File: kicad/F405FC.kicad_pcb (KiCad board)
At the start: 4 copper layers, 36 x 36 mm, 161 parts, among them J1 USB4105-GF-A, J2 ESC, J3 HD VTX, J4 GPS, J5 ELRS, P1 VBAT, P10 LED_DIN, P11 5V, P12 GND, P13 5V, P14 BUZ_N, P15 UART5_TX, P16 UART5_RX, P17 UART6_TX, P18 UART6_RX, P19 MOTOR5, P2 GND, P20 MOTOR6, P21 MOTOR7, P22 MOTOR8, P23 RSSI_IN, P24 GND, P25 5V, P3 10V, P4 GND, P5 CAM1_VID, P6 CAM2_VID, P7 VTX_VID, P8 5V, P9 GND, Q1 PMV40UN2, Q2 NX7002AK, SW1 BOOT, U1 LMR38020FSDDAR, U10 W25N01GV, U11 TS5A3159A, U12 SN74LV1T125, U13 USBLC6-2SC6, U2 LMR38020FSDDAR, U3 STM32F405RGT6, U4 LP38692MP-3.3, U5 LP5907MFX-3.3, U6 ICM-42688-P, U7 BMI270, U8 BMP390, U9 IIS2MDC, Y1 8MHz

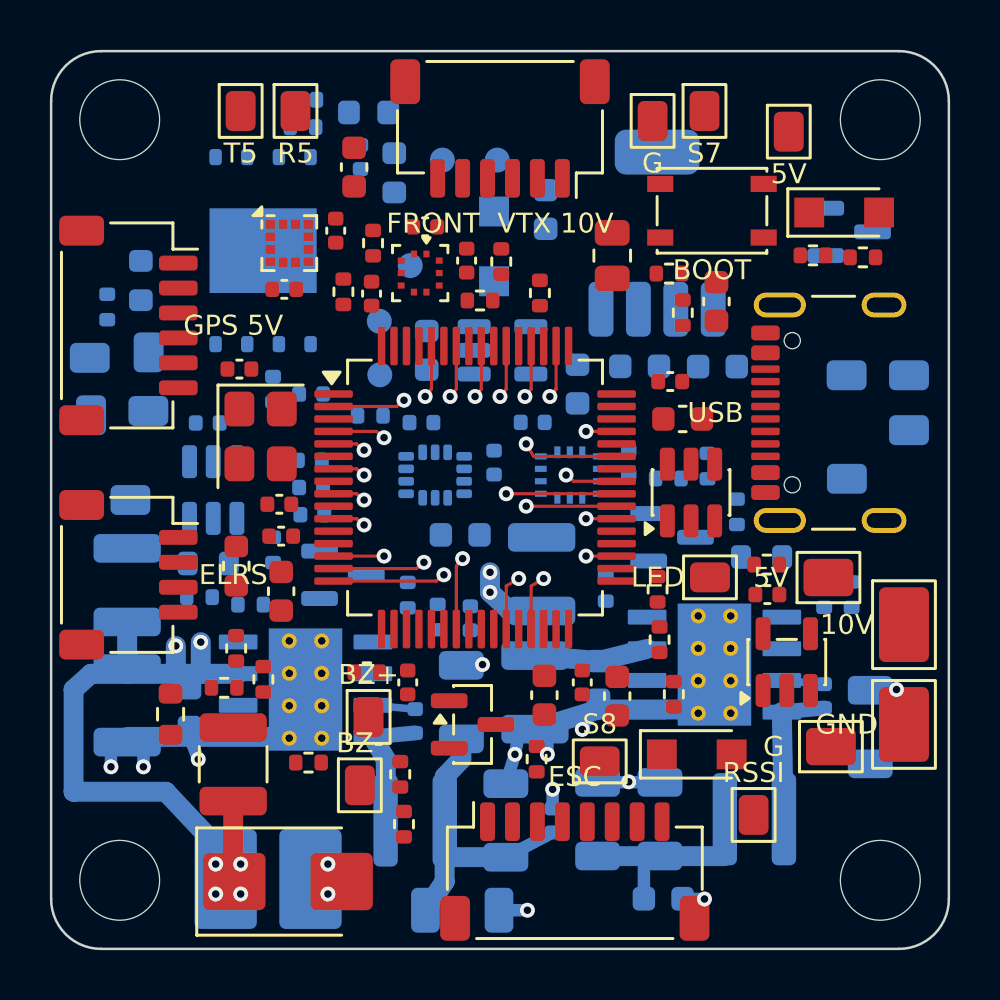
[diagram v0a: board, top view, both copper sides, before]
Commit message: Gate 3 re-review fixes: rule-based labels + regular pad grids, VBAT In2 zone, MCU routing ring/decap offsets, U13/D9 moves, P12 removed (D-21)
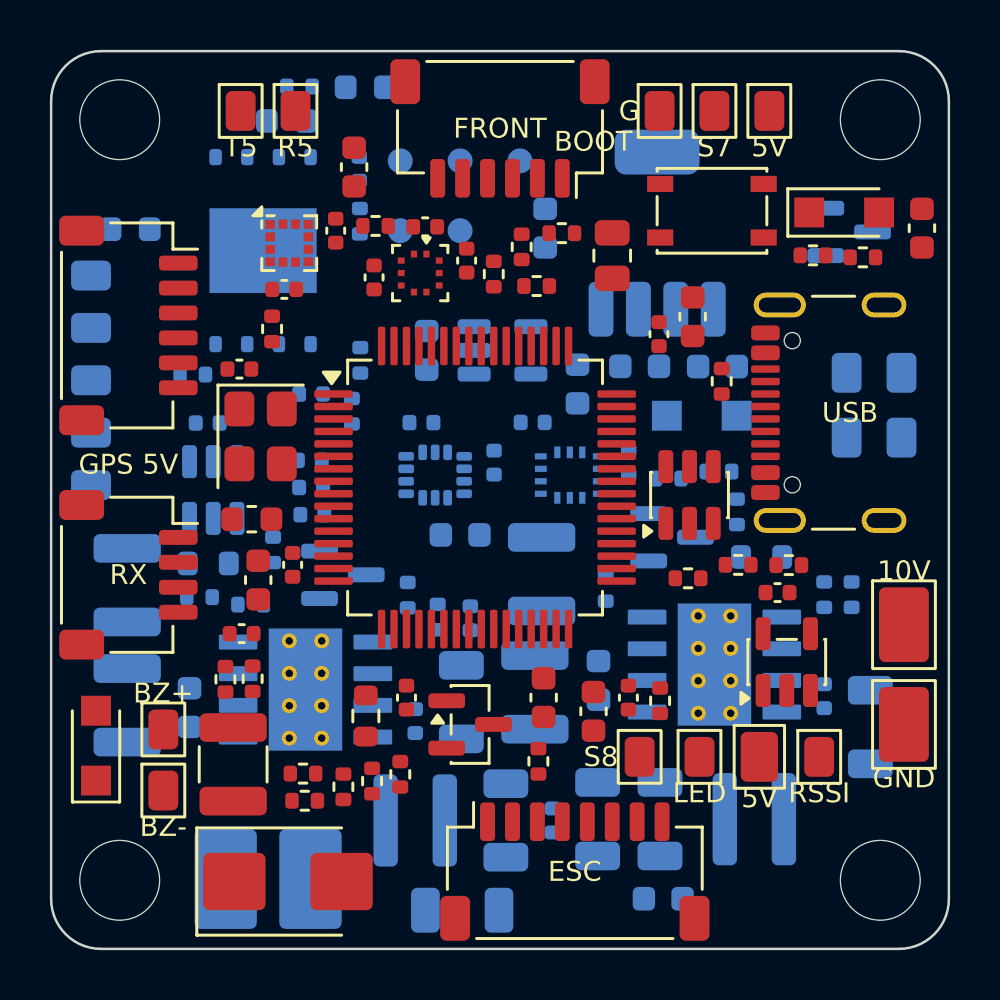
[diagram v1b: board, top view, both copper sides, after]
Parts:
- removed P12: GND, F405FC:Pad_SMD_1.5x2.0mm
- moved D9 24.1 mm to (101.8, 127.8), turned to 90 degrees
- moved D5 10.7 mm to (126.1, 114.6), turned to 0 degrees
- moved C51 8.75 mm to (134.9, 107.1)
- moved P13 8.25 mm to (104.5, 127.2)
- moved P14 7.88 mm to (104.5, 129.7)
- moved R14 7.83 mm to (112.6, 126.7)
- moved P11 7.71 mm to (128.4, 128.3), turned to 0 degrees
- moved P10 7.21 mm to (126.0, 128.3), turned to 0 degrees
- moved P9 7.08 mm to (101.6, 111.1)
- moved TP5 6.62 mm to (116.4, 107.2)
- moved TP3 6.08 mm to (118.8, 104.4)
- moved P8 5.90 mm to (101.6, 109.0)
- moved P7 5.80 mm to (101.6, 117.4), turned to 90 degrees
- moved R32 5.80 mm to (127.5, 120.6), turned to 180 degrees
- moved C37 5.41 mm to (107.6, 123.4)
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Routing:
- net VBAT: track 48.1 -> 0.00 mm, vias 8 -> 0
- net GND: track 26.6 -> 0.00 mm, vias 14 -> 0
- net 5V: track 10.5 -> 0.00 mm
- net 10V: track 6.81 -> 0.00 mm
- net SW_10V: track 6.01 -> 0.00 mm
- net SW_5V: track 5.20 -> 0.00 mm
- net UART2_TX: track 4.52 -> 0.00 mm, vias 1 -> 0
- net MOTOR6: track 4.42 -> 0.00 mm, vias 1 -> 0
- net UART1_RX: track 3.91 -> 0.00 mm, vias 1 -> 0
- net ESC_TLM: track 3.72 -> 0.00 mm, vias 1 -> 0
- net MOTOR5: track 3.62 -> 0.00 mm, vias 1 -> 0
- net CAM_SEL: track 2.92 -> 0.00 mm, vias 1 -> 0
- net SPI1_MOSI: track 2.92 -> 0.00 mm, vias 1 -> 0
- net MOTOR3: track 2.31 -> 0.00 mm, vias 1 -> 0
- net MOTOR2: track 2.31 -> 0.00 mm, vias 1 -> 0
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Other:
- board text added: "FRONT"
- board text added: "RX"
- board text removed: "ELRS"
- board text removed: "FRONT VTX 10V"

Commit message: Routing: PathFinder router, reachability pre-check, fanout stub crossing fix + IMU via keepout
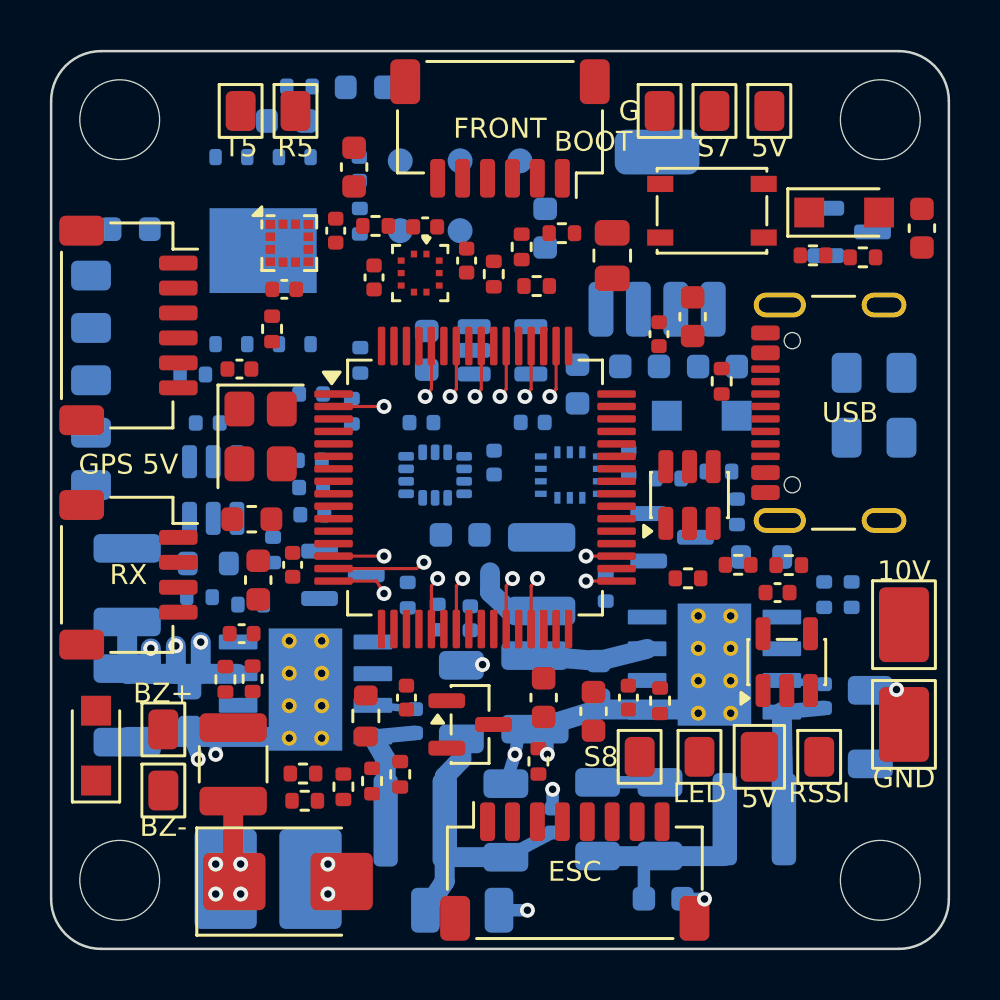
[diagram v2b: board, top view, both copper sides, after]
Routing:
- net GND: track 0.00 -> 24.6 mm, vias 0 -> 11
- net VBAT: track 0.00 -> 22.0 mm, vias 0 -> 7
- net 5V: track 0.00 -> 10.5 mm
- net 10V: track 0.00 -> 6.81 mm
- net SW_10V: track 0.00 -> 6.01 mm
- net SW_5V: track 0.00 -> 5.20 mm
- net ESC_TLM: track 0.00 -> 3.72 mm, vias 0 -> 1
- net UART2_TX: track 0.00 -> 2.31 mm, vias 0 -> 1
- net UART5_RX: track 0.00 -> 2.12 mm, vias 0 -> 1
- net UART3_RX: track 0.00 -> 2.12 mm, vias 0 -> 1
- net SPI3_MISO: track 0.00 -> 2.12 mm, vias 0 -> 1
- net GYRO2_CS: track 0.00 -> 2.12 mm, vias 0 -> 1
- net FLASH_CS: track 0.00 -> 2.12 mm, vias 0 -> 1
- net BOOT0: track 0.00 -> 2.12 mm, vias 0 -> 1
- net SPI1_SCK: track 0.00 -> 2.12 mm, vias 0 -> 1
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- added copper zone on In1.Cu, net GND
- added copper zone on In2.Cu, net VBAT

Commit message: PathFinder: conservative grid margins, string pulling, cost-based window choice, optional In1 hops; power.md §5 rev C; current-limit floors in script (G3R-08)
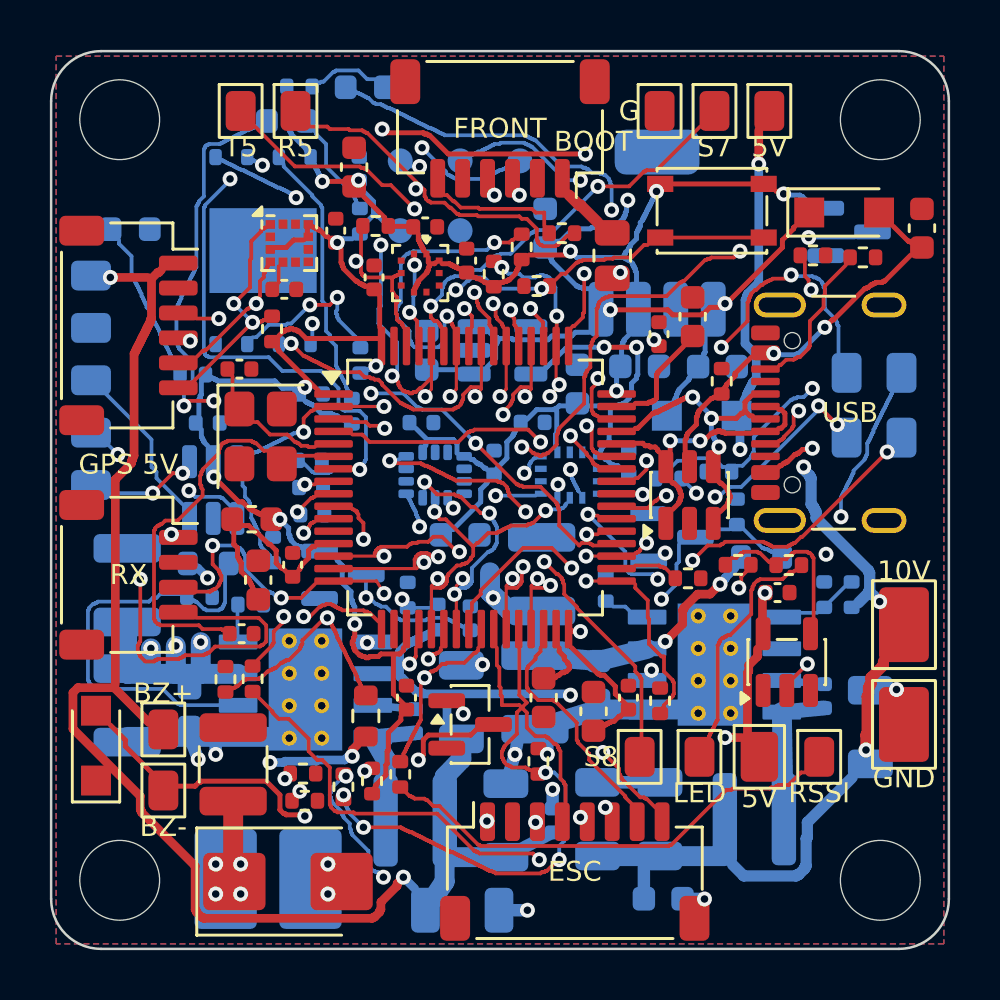
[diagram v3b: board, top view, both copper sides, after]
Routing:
- net 5V: track 10.5 -> 95.0 mm, vias 0 -> 7
- net 3V3: track 0.00 -> 82.3 mm, vias 0 -> 14
- net 5V_SYS: track 0.00 -> 58.6 mm, vias 0 -> 6
- net CURR_ADC: track 0.00 -> 47.3 mm, vias 0 -> 5
- net STATUS_LED_GREEN: track 0.00 -> 33.6 mm, vias 0 -> 4
- net NRST: track 0.00 -> 32.5 mm, vias 0 -> 3
- net 10V: track 6.81 -> 36.2 mm, vias 0 -> 4
- net STATUS_LED_BLUE: track 1.22 -> 29.3 mm, vias 1 -> 3
- net UART2_RX: track 0.00 -> 23.5 mm, vias 0 -> 2
- net BOOT0: track 2.12 -> 25.2 mm, vias 1 -> 5
- net 3V3_IMU: track 0.00 -> 22.9 mm, vias 0 -> 2
- net VTX_OFF_G: track 0.00 -> 21.8 mm, vias 0 -> 3
- net BEEPER: track 0.00 -> 21.0 mm, vias 0 -> 4
- net UART5_RX: track 2.12 -> 23.0 mm, vias 1 -> 3
- net ESC_TLM: track 3.72 -> 22.7 mm, vias 1 -> 3
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- added copper zone on B.Cu, net GND
- added copper zone on F.Cu, net GND
- added copper zone on In2.Cu, net GND

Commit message: Placement tweaks for routability (U5/C23/C53/R21/R22), pairwise clearance + hole clearance in router, GND plane-tie pass, route pipeline script
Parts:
- C53: moved to F.Cu
- R21, R22: moved to B.Cu
- moved R21 14.1 mm to (108.6, 114.9), turned to 180 degrees
- moved R22 13.0 mm to (108.8, 117.1), turned to 90 degrees
- moved C53 6.89 mm to (113.0, 128.5)
- moved R14 3.32 mm to (110.5, 129.2), turned to 180 degrees
- moved R18 2.86 mm to (113.1, 126.4)
- moved R40 2.86 mm to (114.2, 131.0)
- moved U5 1.66 mm to (118.5, 110.4)
- moved C23 1.46 mm to (119.7, 113.0), turned to 0 degrees
- moved C22 1.23 mm to (115.6, 110.9)
- moved C42 0.94 mm to (120.2, 114.9)
- moved C18 0.15 mm to (119.7, 107.1)
- moved R39 0.10 mm to (114.1, 129.0)
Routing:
- net 5V: track 95.0 -> 10.5 mm, vias 7 -> 0
- net 3V3: track 82.3 -> 0.00 mm, vias 14 -> 0
- net 5V_SYS: track 58.6 -> 0.00 mm, vias 6 -> 0
- net CURR_ADC: track 47.3 -> 0.00 mm, vias 5 -> 0
- net STATUS_LED_GREEN: track 33.6 -> 0.00 mm, vias 4 -> 0
- net NRST: track 32.5 -> 0.00 mm, vias 3 -> 0
- net 10V: track 36.2 -> 6.81 mm, vias 4 -> 0
- net STATUS_LED_BLUE: track 29.3 -> 1.22 mm, vias 3 -> 1
- net BOOT0: track 25.2 -> 0.00 mm, vias 5 -> 0
- net UART2_RX: track 23.5 -> 0.00 mm, vias 2 -> 0
- net 3V3_IMU: track 22.9 -> 0.00 mm, vias 2 -> 0
- net VTX_OFF_G: track 21.8 -> 0.00 mm, vias 3 -> 0
- net BEEPER: track 21.0 -> 0.00 mm, vias 4 -> 0
- net UART5_RX: track 23.0 -> 2.12 mm, vias 3 -> 1
- net FLASH_CS: track 19.7 -> 0.00 mm, vias 4 -> 0
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- removed copper zone on B.Cu, net GND
- removed copper zone on F.Cu, net GND
- removed copper zone on In2.Cu, net GND

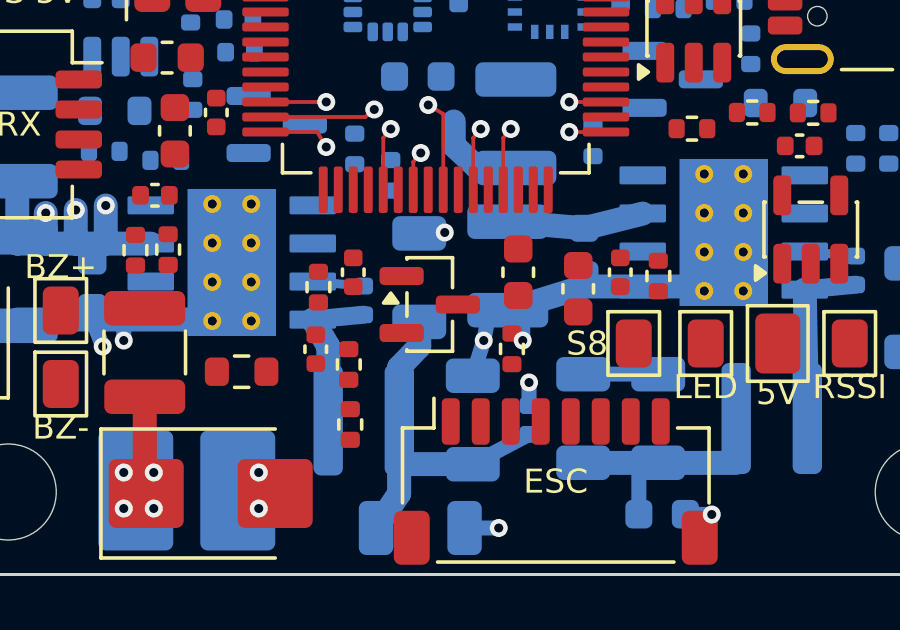
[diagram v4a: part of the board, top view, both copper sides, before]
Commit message: Legalizer keeps non-anchored parts off scripted critical copper; narrower lower VBAT riser; configurable routing grid
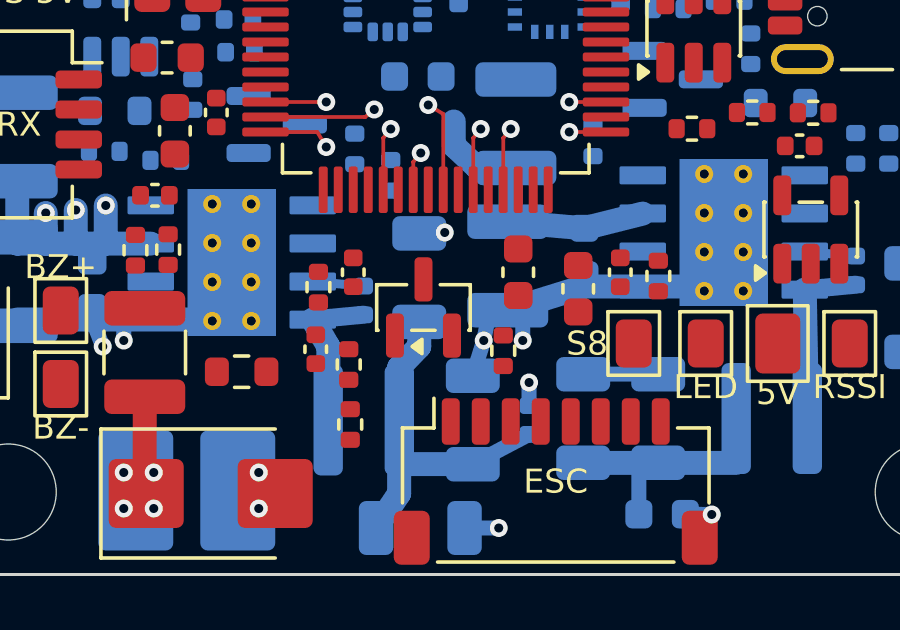
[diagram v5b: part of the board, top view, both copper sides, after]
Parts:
- moved R17 0.30 mm to (119.2, 128.5)
- moved Q1 0.23 mm to (116.6, 127.1), turned to 90 degrees

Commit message: D-23: ADC clamp diodes removed (routing space under the MCU corner); BOM $174.68; PathFinder RESET_NETS
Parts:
- removed D7, D8: BAT54S, Package_TO_SOT_SMD:SOT-23
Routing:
- net ESC_TLM: track 3.72 -> 1.32 mm
- net UART2_TX: track 2.31 -> 0.00 mm, vias 1 -> 0
- net SPI1_MISO: track 0.00 -> 2.31 mm, vias 0 -> 1
- net SPI1_MOSI: track 1.32 -> 0.00 mm, vias 1 -> 0
- net UART2_RX: track 0.00 -> 1.22 mm, vias 0 -> 1
- net GYRO1_INT: track 0.00 -> 1.22 mm, vias 0 -> 1

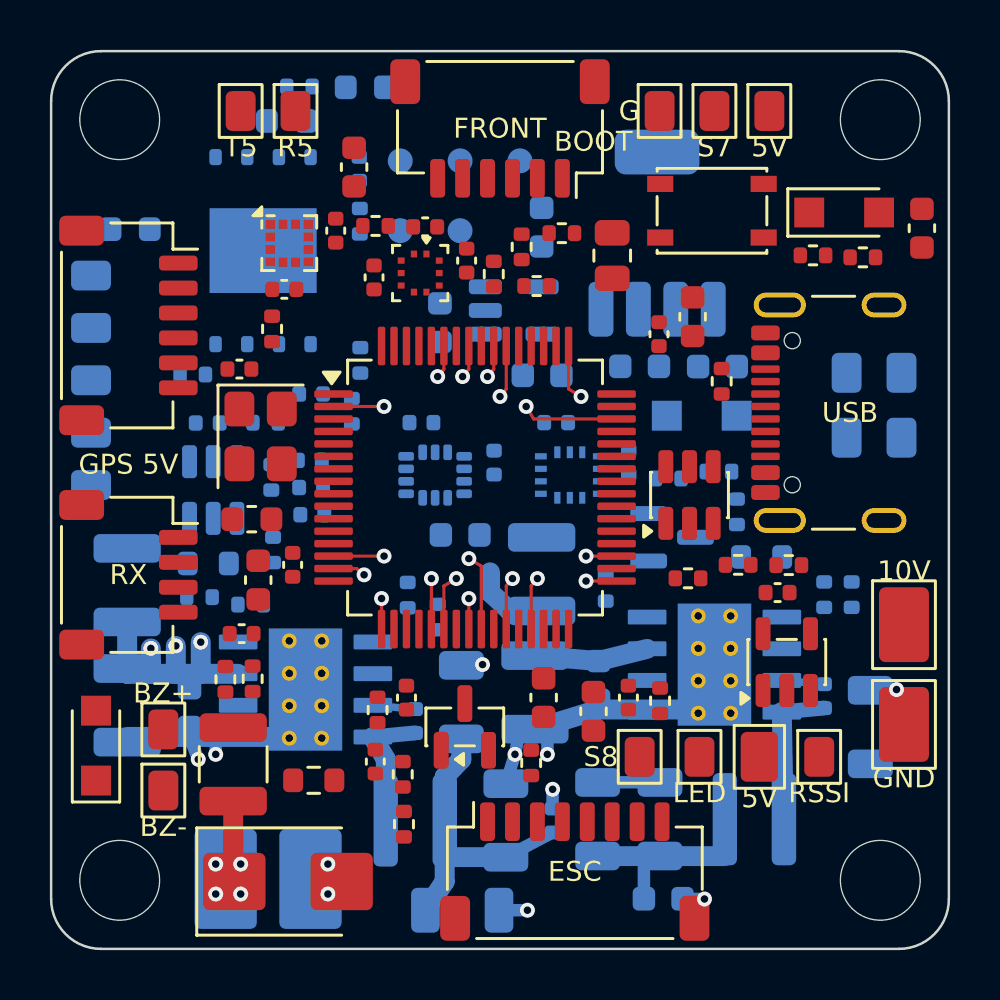
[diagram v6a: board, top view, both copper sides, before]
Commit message: Routing: PathFinder router, fine grid + In1 hops, GND pass, solid SMD pour connections (WIP: 2 DRC errors, 26 opens)
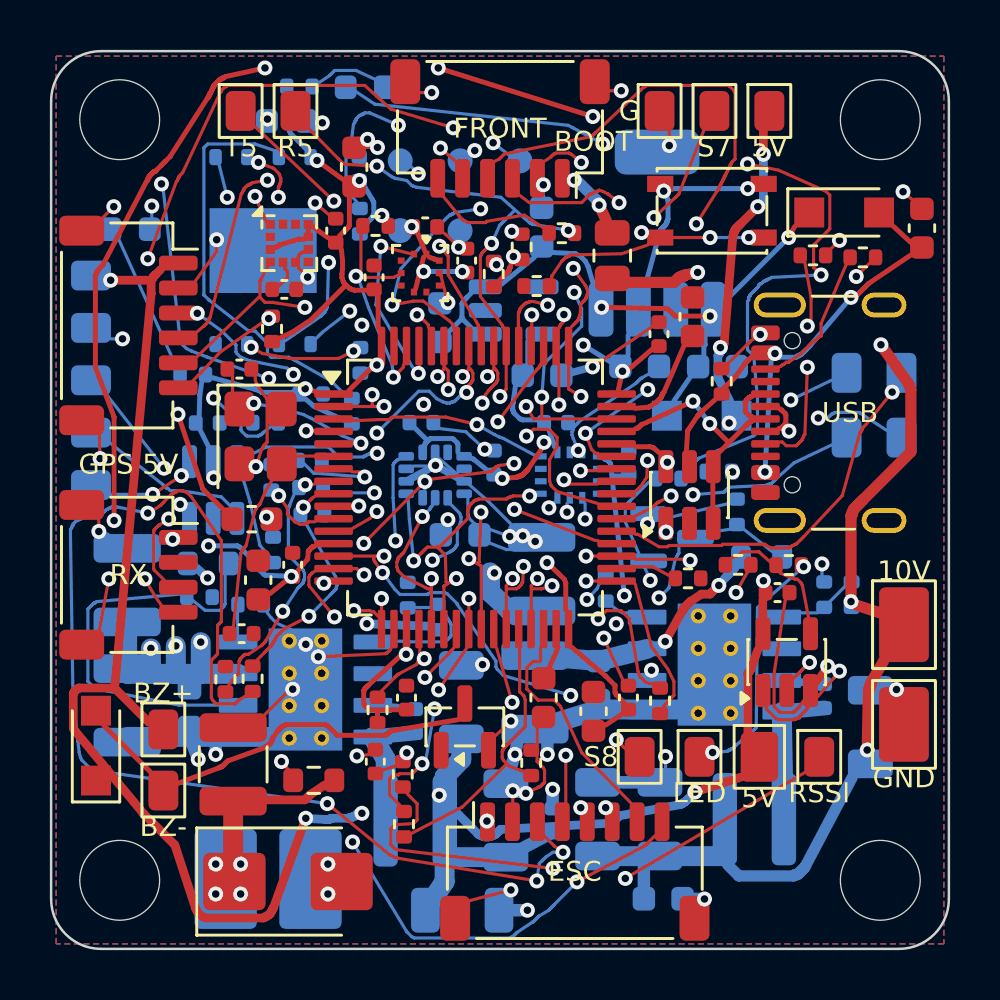
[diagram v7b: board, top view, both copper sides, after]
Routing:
- net GND: track 24.6 -> 116.4 mm, vias 11 -> 60
- net 5V: track 10.5 -> 101.2 mm, vias 0 -> 11
- net 3V3: track 0.00 -> 81.6 mm, vias 0 -> 17
- net 5V_SYS: track 0.00 -> 63.1 mm, vias 0 -> 8
- net VTX_PWR_EN: track 0.00 -> 58.7 mm, vias 0 -> 3
- net ESC_CURR: track 0.00 -> 47.3 mm, vias 0 -> 4
- net NRST: track 0.00 -> 38.0 mm, vias 0 -> 4
- net 10V: track 6.81 -> 42.3 mm, vias 0 -> 4
- net 3V3_IMU: track 0.00 -> 33.4 mm, vias 0 -> 4
- net STATUS_LED_BLUE: track 1.22 -> 34.1 mm, vias 1 -> 3
- net STATUS_LED_GREEN: track 0.00 -> 31.5 mm, vias 0 -> 4
- net ESC_TLM: track 1.32 -> 29.3 mm, vias 1 -> 4
- net UART1_RX: track 0.00 -> 27.6 mm, vias 0 -> 3
- net I2C1_SCL: track 0.00 -> 23.8 mm, vias 0 -> 4
- net RSSI_IN: track 0.00 -> 21.0 mm, vias 0 -> 2
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- added copper zone on B.Cu, net GND
- added copper zone on F.Cu, net GND
- added copper zone on In2.Cu, net GND
